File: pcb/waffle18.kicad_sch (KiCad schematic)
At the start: 38 parts

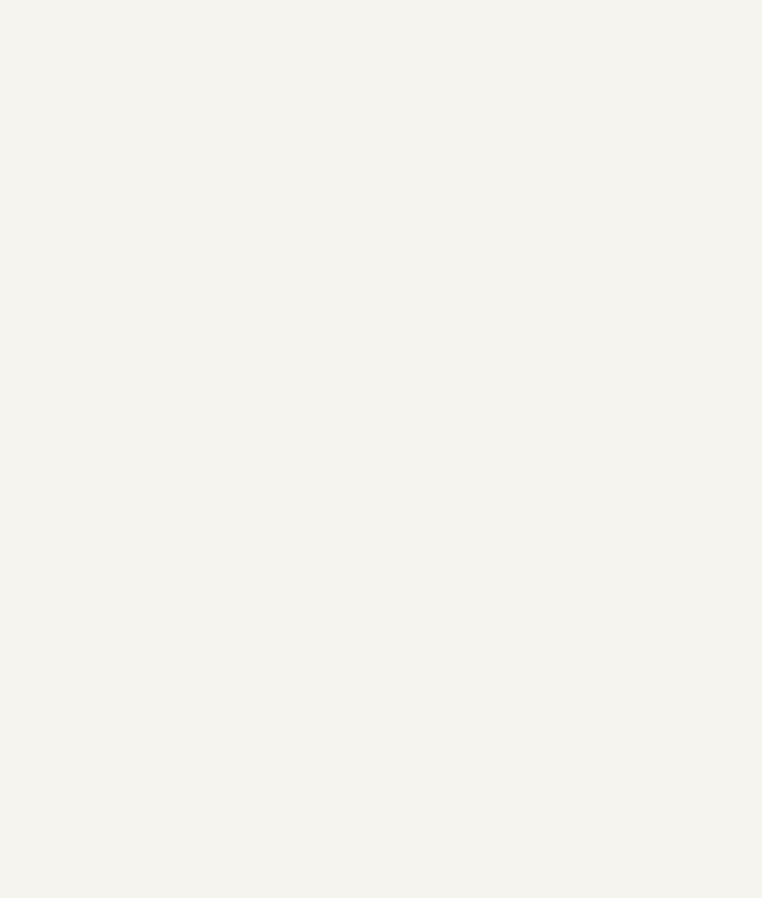
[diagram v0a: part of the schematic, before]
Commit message: feat(schematic): connect matrix to XIAO RP2350
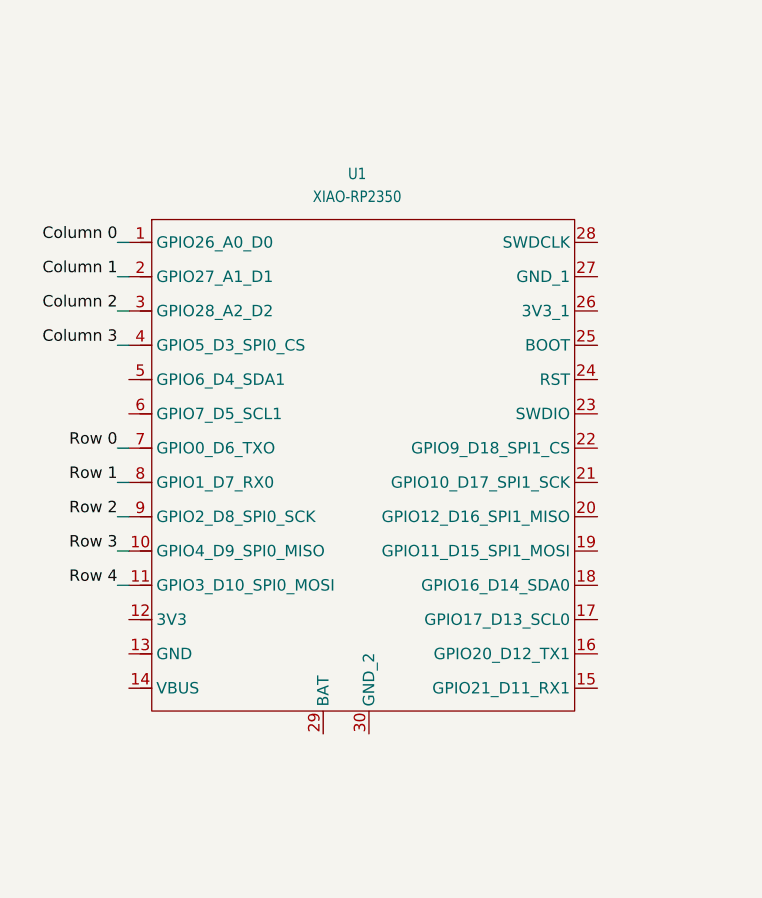
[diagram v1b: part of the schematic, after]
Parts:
- added U1: XIAO-RP2350, waffle18-mcu:XIAO_DIP, symbol waffle18:XIAO-RP2350
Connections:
- net Column 0: now also U1.1 (GPIO26_A0_D0)
- net Column 1: now also U1.2 (GPIO27_A1_D1)
- net Column 2: now also U1.3 (GPIO28_A2_D2)
- net Column 3: now also U1.4 (GPIO5_D3_SPI0_CS)
- net Row 0: now also U1.7 (GPIO0_D6_TXO)
- net Row 1: now also U1.8 (GPIO1_D7_RX0)
- net Row 2: now also U1.9 (GPIO2_D8_SPI0_SCK)
- net Row 3: now also U1.10 (GPIO4_D9_SPI0_MISO)
- net Row 4: now also U1.11 (GPIO3_D10_SPI0_MOSI)

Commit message: feat(schematic): assign switch and stabilizer footprints
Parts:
- S1, S10, S11, S12, S13, S14, S15, S16, S17, S2, S3, S4, S5, S6, S7, S8: footprint (none) -> waffle18-switch:MX_KS-2P02B01-01_1.00u
- S18: footprint (none) -> waffle18-switch:MX_KS-2P02B01-01_2.00u-H
- S9: footprint (none) -> waffle18-switch:MX_KS-2P02B01-01_2.00u-V
- STAB1, STAB2: footprint (none) -> waffle18-stabilizer:STAB_MX_2.00u
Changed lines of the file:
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@@
 			)
 		)
-		(property "Footprint" ""
+		(property "Footprint" "waffle18-switch:MX_KS-2P02B01-01_1.00u"
 			(at 205.74 97.282 0)
 			(hide yes)
@@
 			)
 		)
-		(property "Footprint" ""
+		(property "Footprint" "waffle18-switch:MX_KS-2P02B01-01_1.00u"
 			(at 193.04 97.282 0)
 			(hide yes)
@@
 			)
 		)
-		(property "Footprint" ""
+		(property "Footprint" "waffle18-stabilizer:STAB_MX_2.00u"
 			(at 214.63 135.89 0)
 			(hide yes)
@@
 			)
 		)
-		(property "Footprint" ""
+		(property "Footprint" "waffle18-switch:MX_KS-2P02B01-01_1.00u"
 			(at 218.44 78.232 0)
 			(hide yes)
@@
 			)
 		)
-		(property "Footprint" ""
+		(property "Footprint" "waffle18-switch:MX_KS-2P02B01-01_2.00u-V"
 			(at 180.34 97.282 0)
 			(hide yes)
@@
 			)
 		)
-		(property "Footprint" ""
+		(property "Footprint" "waffle18-switch:MX_KS-2P02B01-01_1.00u"
 			(at 193.04 116.332 0)
 			(hide yes)
@@
 			)
 		)
-		(property "Footprint" ""
+		(property "Footprint" "waffle18-switch:MX_KS-2P02B01-01_1.00u"
 			(at 180.34 59.182 0)
 			(hide yes)
@@
 			)
 		)
-		(property "Footprint" ""
+		(property "Footprint" "waffle18-switch:MX_KS-2P02B01-01_1.00u"
 			(at 193.04 59.182 0)
 			(hide yes)
@@
 			)
 		)
-		(property "Footprint" ""
+		(property "Footprint" "waffle18-switch:MX_KS-2P02B01-01_1.00u"
 			(at 218.44 116.332 0)
 			(hide yes)
@@
 			)
 		)
-		(property "Footprint" ""
+		(property "Footprint" "waffle18-switch:MX_KS-2P02B01-01_2.00u-H"
 			(at 218.44 135.382 0)
 			(hide yes)
@@
 			)
 		)
-		(property "Footprint" ""
+		(property "Footprint" "waffle18-switch:MX_KS-2P02B01-01_1.00u"
 			(at 218.44 97.282 0)
 			(hide yes)
@@
 			)
 		)
-		(property "Footprint" ""
+		(property "Footprint" "waffle18-switch:MX_KS-2P02B01-01_1.00u"
 			(at 180.34 135.382 0)
 			(hide yes)
@@
 			)
 		)
-		(property "Footprint" ""
+		(property "Footprint" "waffle18-switch:MX_KS-2P02B01-01_1.00u"
 			(at 193.04 135.382 0)
 			(hide yes)
@@
 			)
 		)
-		(property "Footprint" ""
+		(property "Footprint" "waffle18-switch:MX_KS-2P02B01-01_1.00u"
 			(at 205.74 78.232 0)
 			(hide yes)
@@
 			)
 		)
-		(property "Footprint" ""
+		(property "Footprint" "waffle18-switch:MX_KS-2P02B01-01_1.00u"
 			(at 193.04 78.232 0)
 			(hide yes)
@@
 			)
 		)
-		(property "Footprint" ""
+		(property "Footprint" "waffle18-switch:MX_KS-2P02B01-01_1.00u"
 			(at 205.74 59.182 0)
 			(hide yes)
@@
 			)
 		)
-		(property "Footprint" ""
+		(property "Footprint" "waffle18-switch:MX_KS-2P02B01-01_1.00u"
 			(at 205.74 116.332 0)
 			(hide yes)
@@
 			)
 		)
-		(property "Footprint" ""
+		(property "Footprint" "waffle18-switch:MX_KS-2P02B01-01_1.00u"
 			(at 218.44 59.182 0)
 			(hide yes)
@@
 			)
 		)
-		(property "Footprint" ""
+		(property "Footprint" "waffle18-switch:MX_KS-2P02B01-01_1.00u"
 			(at 180.34 78.232 0)
 			(hide yes)
@@
 			)
 		)
-		(property "Footprint" ""
+		(property "Footprint" "waffle18-stabilizer:STAB_MX_2.00u"
 			(at 184.15 111.76 0)
 			(hide yes)

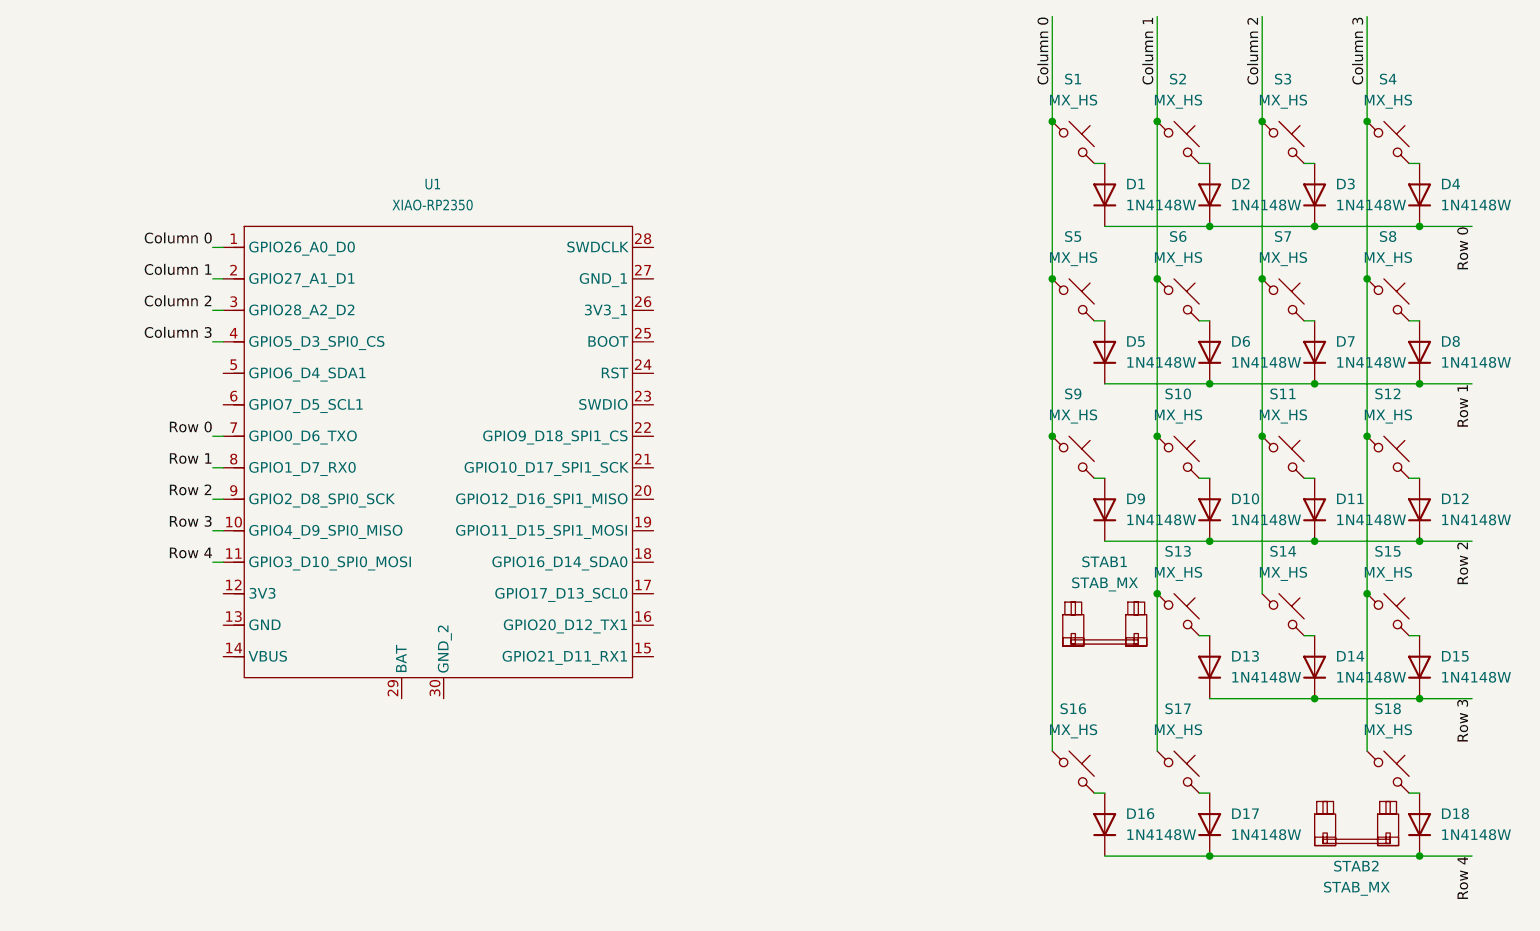
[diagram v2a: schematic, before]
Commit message: refactor(schematic): optimize pin assignment for routing
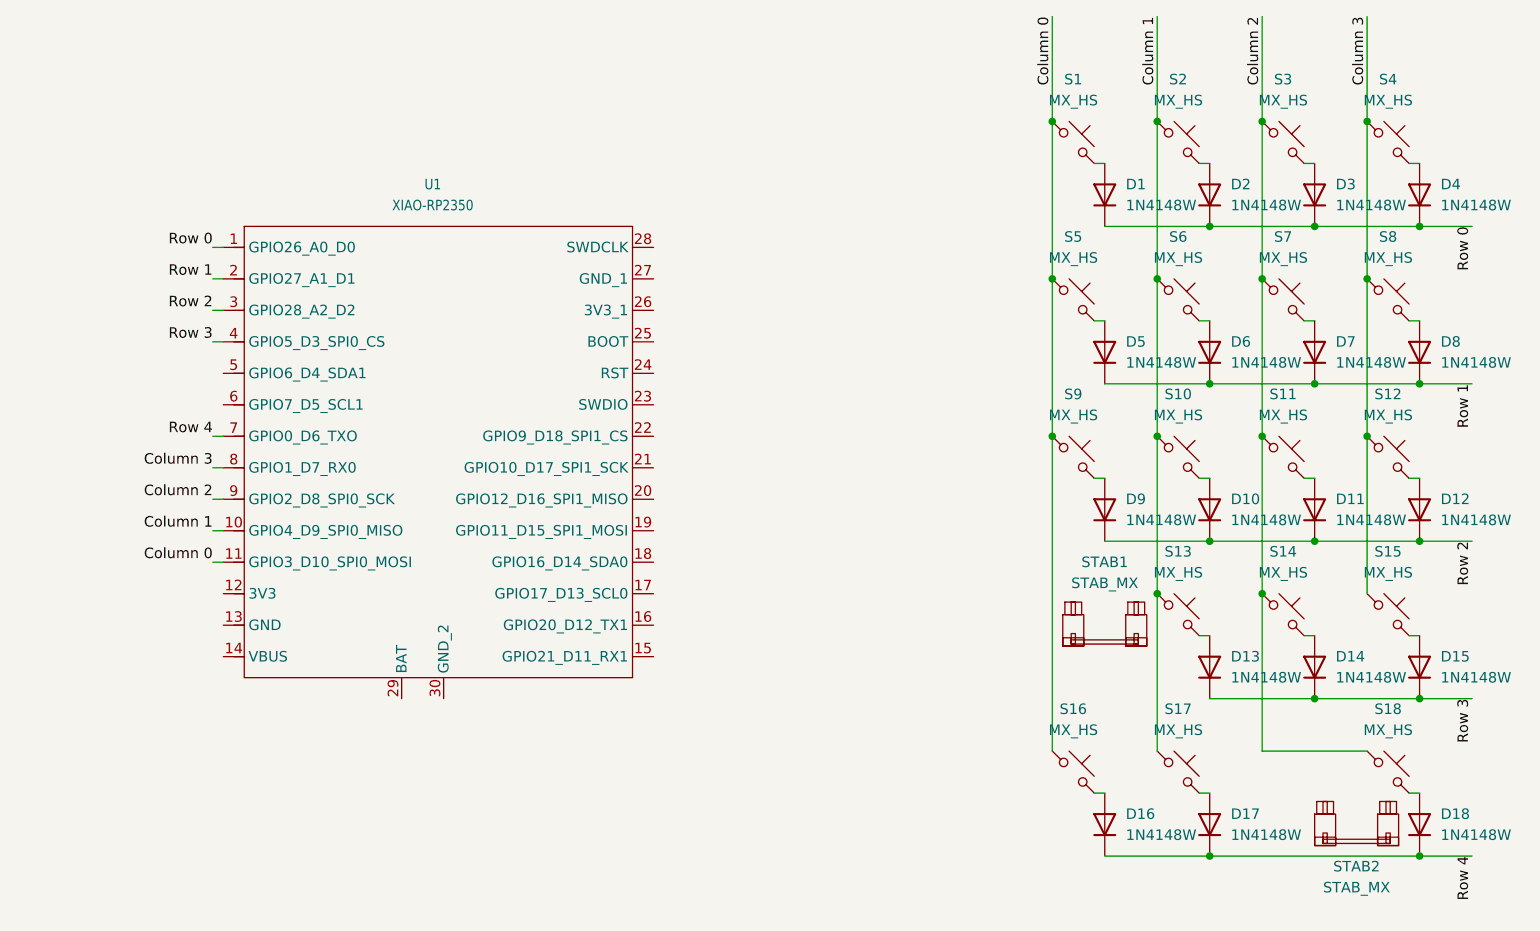
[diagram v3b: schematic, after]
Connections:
- net Column 0: now also U1.11 (GPIO3_D10_SPI0_MOSI); no longer U1.1 (GPIO26_A0_D0)
- net Column 1: now also U1.10 (GPIO4_D9_SPI0_MISO); no longer U1.2 (GPIO27_A1_D1)
- net Column 2: now also S18.1, U1.9 (GPIO2_D8_SPI0_SCK); no longer U1.3 (GPIO28_A2_D2)
- net Column 3: now also U1.8 (GPIO1_D7_RX0); no longer S18.1, U1.4 (GPIO5_D3_SPI0_CS)
- net Row 0: now also U1.1 (GPIO26_A0_D0); no longer U1.7 (GPIO0_D6_TXO)
- net Row 1: now also U1.2 (GPIO27_A1_D1); no longer U1.8 (GPIO1_D7_RX0)
- net Row 2: now also U1.3 (GPIO28_A2_D2); no longer U1.9 (GPIO2_D8_SPI0_SCK)
- net Row 3: now also U1.4 (GPIO5_D3_SPI0_CS); no longer U1.10 (GPIO4_D9_SPI0_MISO)
- net Row 4: now also U1.7 (GPIO0_D6_TXO); no longer U1.11 (GPIO3_D10_SPI0_MOSI)

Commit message: chore(pcb): prepare for production
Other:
- title: (none) -> waffle18
- moved on the sheet: U1
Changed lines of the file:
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@@
 	(generator "eeschema")
 	(generator_version "10.0")
-	(paper "A4")
+	(paper "USLetter")
+	(title_block
+		(title "waffle18")
+		(date "2026-05-10")
+		(rev "0.1")
+	)
 	(junction
 		(at 203.2 107.95)
@@
 	(wire
 		(pts
-			(xy 76.2 100.33) (xy 77.47 100.33)
+			(xy 63.5 100.33) (xy 64.77 100.33)
 		)
 		(stroke
@@
 	(wire
 		(pts
-			(xy 76.2 66.04) (xy 77.47 66.04)
+			(xy 63.5 66.04) (xy 64.77 66.04)
 		)
 		(stroke
@@
 	(wire
 		(pts
-			(xy 76.2 73.66) (xy 77.47 73.66)
+			(xy 63.5 73.66) (xy 64.77 73.66)
 		)
 		(stroke
@@
 	(wire
 		(pts
-			(xy 76.2 96.52) (xy 77.47 96.52)
+			(xy 63.5 96.52) (xy 64.77 96.52)
 		)
 		(stroke
@@
 	(wire
 		(pts
-			(xy 76.2 88.9) (xy 77.47 88.9)
+			(xy 63.5 88.9) (xy 64.77 88.9)
 		)
 		(stroke
@@
 	(wire
 		(pts
-			(xy 76.2 104.14) (xy 77.47 104.14)
+			(xy 63.5 104.14) (xy 64.77 104.14)
 		)
 		(stroke
@@
 	(wire
 		(pts
-			(xy 76.2 69.85) (xy 77.47 69.85)
+			(xy 63.5 69.85) (xy 64.77 69.85)
 		)
 		(stroke
@@
 	(wire
 		(pts
-			(xy 76.2 77.47) (xy 77.47 77.47)
+			(xy 63.5 77.47) (xy 64.77 77.47)
 		)
 		(stroke
@@
 	(wire
 		(pts
-			(xy 76.2 92.71) (xy 77.47 92.71)
+			(xy 63.5 92.71) (xy 64.77 92.71)
 		)
 		(stroke
@@
 	)
 	(label "Row 1"
-		(at 76.2 69.85 180)
+		(at 63.5 69.85 180)
 		(effects
 			(font
@@
 	)
 	(label "Column 3"
-		(at 76.2 92.71 180)
+		(at 63.5 92.71 180)
 		(effects
 			(font
@@
 	)
 	(label "Row 2"
-		(at 76.2 73.66 180)
+		(at 63.5 73.66 180)
 		(effects
 			(font
@@
 	)
 	(label "Column 0"
-		(at 76.2 104.14 180)
+		(at 63.5 104.14 180)
 		(effects
 			(font
@@
 	)
 	(label "Row 0"
-		(at 76.2 66.04 180)
+		(at 63.5 66.04 180)
 		(effects
 			(font
@@
 	)
 	(label "Row 4"
-		(at 76.2 88.9 180)
+		(at 63.5 88.9 180)
 		(effects
 			(font
@@
 	)
 	(label "Row 3"
-		(at 76.2 77.47 180)
+		(at 63.5 77.47 180)
 		(effects
 			(font
@@
 	)
 	(label "Column 2"
-		(at 76.2 96.52 180)
+		(at 63.5 96.52 180)
 		(effects
 			(font
@@
 	)
 	(label "Column 1"
-		(at 76.2 100.33 180)
+		(at 63.5 100.33 180)
 		(effects
 			(font
@@
 	(symbol
 		(lib_id "waffle18:XIAO-RP2350")
-		(at 101.6 88.9 0)
+		(at 88.9 88.9 0)
 		(unit 1)
 		(body_style 1)
@@
 		(fields_autoplaced yes)
 		(property "Reference" "U1"
-			(at 102.8319 58.42 0)
+			(at 90.1319 58.42 0)
 			(show_name no)
 			(do_not_autoplace no)
@@
 		)
 		(property "Value" "XIAO-RP2350"
-			(at 102.8319 60.96 0)
+			(at 90.1319 60.96 0)
 			(show_name no)
 			(do_not_autoplace no)
@@
 		)
 		(property "Footprint" "waffle18-mcu:XIAO_DIP"
-			(at 115.824 62.484 0)
+			(at 103.124 62.484 0)
 			(hide yes)
 			(show_name no)
@@
 		)
 		(property "Datasheet" ""
-			(at 101.6 77.47 0)
+			(at 88.9 77.47 0)
 			(hide yes)
 			(show_name no)
@@
 		)
 		(property "Description" "XIAO-RP2350-SMD by Seeed-Studio/OPL_Kicad_Library on GitHub, used under CC-BY-SA-4.0 / Modified field values"
-			(at 101.6 58.42 0)
+			(at 88.9 58.42 0)
 			(hide yes)
 			(show_name no)
